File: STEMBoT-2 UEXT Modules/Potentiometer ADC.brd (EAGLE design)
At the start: 21.6 x 26.3 mm, 18 parts, among them IC1 74HC165PW,118, IC2 LMV324DR2G, IC3 LMV324DR2G, Q1 MMBT3904LP-7

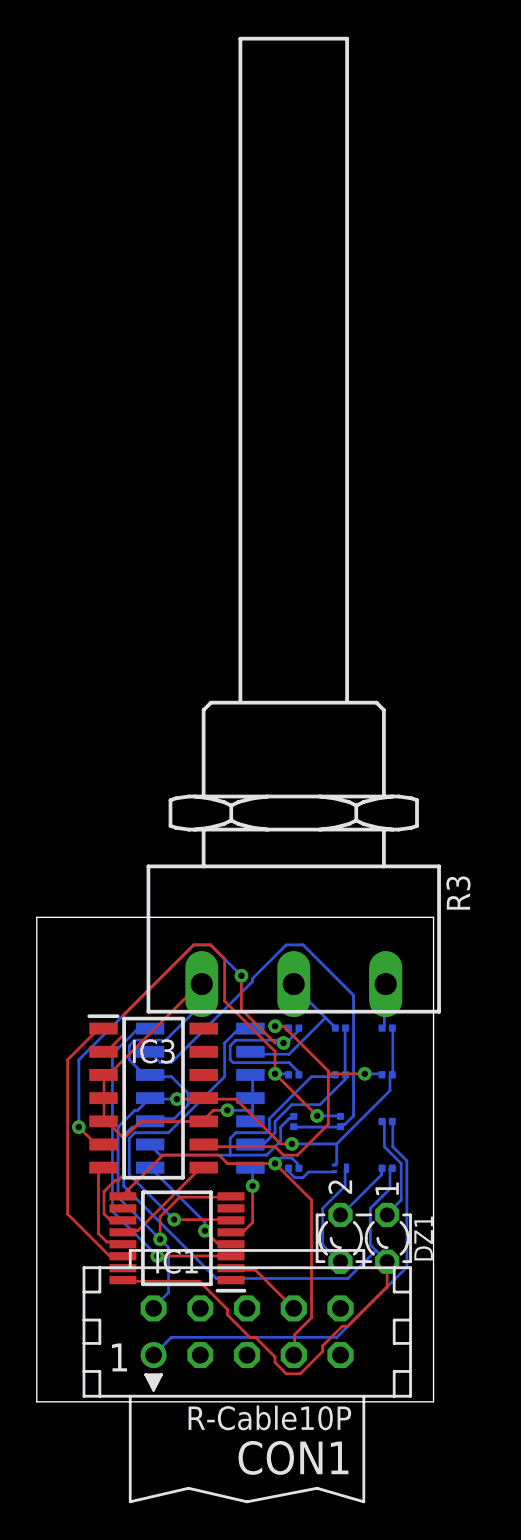
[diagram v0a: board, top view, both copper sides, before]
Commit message: Adjusted ADC modules for PCB order. Dan, these are auto-routed.
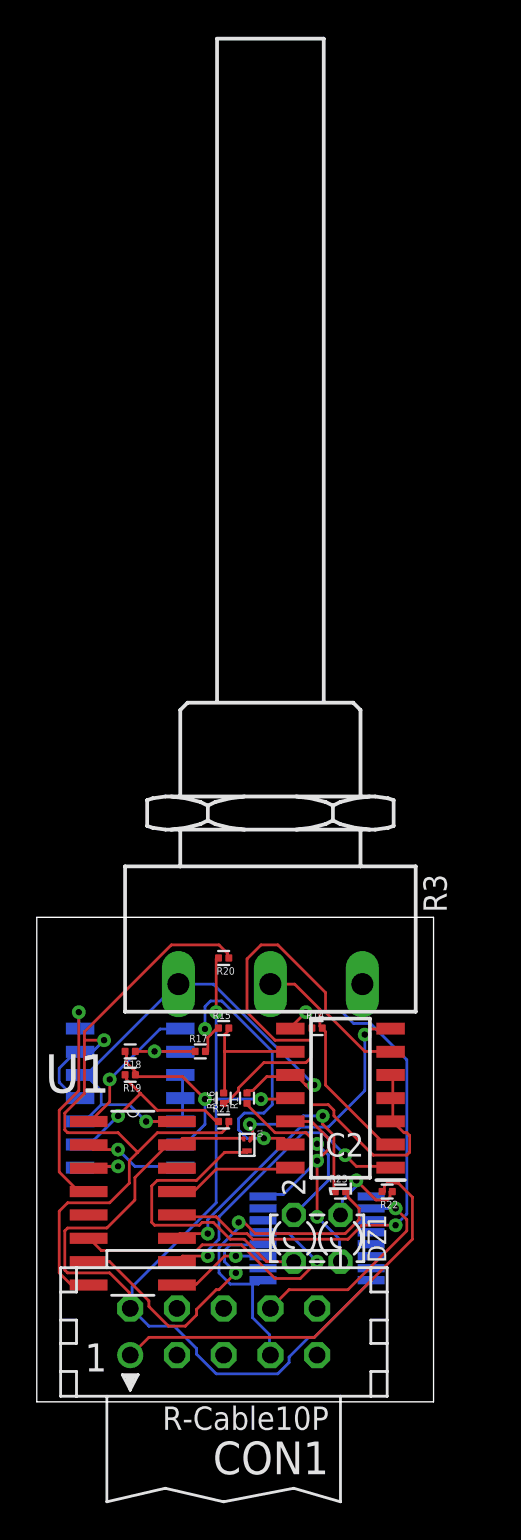
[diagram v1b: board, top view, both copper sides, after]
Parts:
- added U1: SN74HC148D, SN74HC148D:SOIC127P600X175-16N
- moved R20 9.67 mm to (10.2, 24.1), flipped to the top
- moved R19 9.25 mm to (5.08, 17.8), flipped to the top, turned to 180 degrees
- moved R21 9.25 mm to (10.2, 15.2), flipped to the top, turned to 0 degrees
- moved R18 8.98 mm to (5.08, 19.1), flipped to the top
- moved R17 8.52 mm to (8.89, 19.1), flipped to the top, turned to 0 degrees
- moved IC2 7.62 mm to (16.5, 16.5), flipped to the top, turned to 180 degrees
- moved IC1 7.62 mm to (15.2, 8.89), flipped to the bottom, turned to 0 degrees
- moved R16 6.48 mm to (10.2, 16.5), flipped to the top, turned to 90 degrees
- moved R15 6.35 mm to (10.2, 20.3), flipped to the top, turned to 0 degrees
- moved Q1 5.24 mm to (11.4, 14.0), flipped to the top, turned to 270 degrees
- moved R1 4.58 mm to (11.4, 16.5), flipped to the top, turned to 90 degrees
- moved R22 3.81 mm to (19.1, 11.4), flipped to the top
- moved R23 2.84 mm to (16.5, 11.4), flipped to the top
- moved DZ1 2.54 mm to (15.2, 8.89)
- moved R14 1.27 mm to (15.2, 20.3), flipped to the top
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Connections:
- removed net N$2 (its old number): CON1.2, IC1.8, IC2.11, IC3.11, Q1.2, R20.2, R21.2
- removed net N$27: CON1.7, IC1.9, R1.1
- removed net N$30: IC1.3, IC2.14
- new net N$12: CON1.2, IC1.8, IC2.11, Q1.2, R20.2, U1.15
- new net N$16: IC1.13, U1.6
- new net N$19: CON1.7, IC1.9, R23.2
- new net N$20: Q1.1, R23.1
- new net N$22: DZ1.A2, R1.1
- new net N$4: IC2.14, U1.13
- new net N$8: IC1.11, U1.9
- net N$1: now also IC3.11, IC3.13, R20.1, R21.2, U1.8; no longer Q1.1, R1.2
- net N$15: now also IC1.12, U1.7; no longer R20.1, R3.1A
- net N$23: now also U1.2; no longer IC1.13
- net N$26: now also U1.1; no longer IC1.14
- net N$31: now also U1.12; no longer IC1.4
- net N$32: now also U1.11; no longer IC1.5
- net N$33: now also U1.10; no longer IC1.6
- net N$5: now also IC3.12, R1.2, U1.16; no longer IC1.11, R23.1
- net N$6: now also U1.3; no longer IC1.12
- net N$7: now also IC3.14, U1.4; no longer DZ1.A2, R23.2
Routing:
- net N$12: track 0.00 -> 61.9 mm, vias 0 -> 2
- net N$1: track 3.08 -> 44.2 mm, vias 0 -> 1
- net N$2 (its old number): track 39.3 -> 0.00 mm, vias 3 -> 0
- net N$5: track 89.9 -> 62.0 mm, vias 1 -> 4
- net N$9: track 32.2 -> 9.28 mm, vias 3 -> 1
- net N$31: track 6.97 -> 29.8 mm, vias 1 -> 2
- net N$27: track 22.8 -> 0.00 mm, vias 1 -> 0
- net N$19: track 0.00 -> 19.8 mm, vias 0 -> 1
- net N$30: track 18.8 -> 0.00 mm, vias 1 -> 0
- net N$3: track 22.7 -> 4.66 mm, vias 2 -> 1
- net N$16: track 0.00 -> 17.6 mm, vias 0 -> 1
- net N$10: track 9.77 -> 25.7 mm
- net N$32: track 4.59 -> 18.6 mm, vias 1 -> 2
- net N$15: track 2.52 -> 14.7 mm, vias 0 -> 1
- net N$24: track 6.05 -> 16.7 mm
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
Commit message: Once again, updating ADC shematics and boards. Used autorouter.
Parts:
- removed IC2, IC3: LMV324DR2G, LMV324DR2G:SOP126P600X175-14N
- removed R20: ERJ-1RHD3601C, Resistor:RESC0603X26N
- added R2, R4: ERJ-1RHD3601C, Resistor:RESC0603X26N
- added U2, U3: MAX964ESET, MAX964ESET:SOIC127P600X175-16N
- moved R21 9.92 mm to (2.54, 21.6)
- moved R22 8.98 mm to (17.8, 2.54)
- moved R16 8.03 mm to (2.54, 19.1), turned to 180 degrees
- moved R18 5.68 mm to (10.2, 21.6)
- moved R23 5.39 mm to (20.3, 7.62), turned to 270 degrees
- moved R15 5.24 mm to (15.2, 21.6), turned to 180 degrees
- moved Q1 4.58 mm to (15.2, 11.4), turned to 180 degrees
- moved R17 4.58 mm to (5.08, 21.6)
- moved R14 3.81 mm to (15.2, 16.5), turned to 270 degrees
- moved R1 1.80 mm to (10.2, 15.2), turned to 180 degrees
- moved DZ1 1.27 mm to (15.2, 7.62)
- moved IC1 1.27 mm to (15.2, 10.2)
- moved R19 1.27 mm to (5.08, 19.1), turned to 0 degrees
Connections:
- removed net N$17: IC3.9, R19.2, R21.1
- removed net N$31: IC2.8, U1.12
- removed net N$32: IC2.7, U1.11
- removed net N$33: IC2.1, U1.10
- removed net N$5: DZ1.K1, IC1.16, IC2.10, IC2.12, IC2.3, IC2.4, IC2.5, IC3.10, IC3.12, IC3.3, IC3.4, IC3.5, R1.2, R3.1E, U1.16
- new net N$21: U1.2, U2.11
- new net N$27: U1.12, U3.14
- new net N$28: U1.11, U3.11
- new net N$29: U1.10, U3.10
- new net N$30: DZ1.K1, IC1.16, R1.2, R3.1E, R3.1S, R4.2, U1.16, U2.13, U2.2, U2.4, U2.6, U2.8, U3.13, U3.2, U3.4, U3.6, U3.8
- net N$1: now also R16.1, R2.2, U3.5; no longer IC3.11, IC3.13, R20.1, R21.2, U1.8
- net N$10: now also R16.2, R21.1, U3.3; no longer IC2.6, R14.1, R16.1
- net N$11: now also R19.1, R2.1, U3.7; no longer IC2.2, R14.2, R3.1S
- net N$12: now also R19.2, U1.8, U2.12, U3.12; no longer IC2.11, R20.2
- net N$13: now also U1.4, U2.15; no longer IC2.9, R15.2, R16.2
- net N$14: now also U1.3, U2.14; no longer IC2.13, R15.1, R17.2
- net N$23: now also U1.13, U2.10; no longer IC3.7, U1.2
- net N$26: now also U3.15; no longer IC3.1
- net N$3: now also R14.2, R4.1, U2.1; no longer IC3.2, R17.1, R18.1
- net N$4: now also R14.1, R15.1, U2.3; no longer IC2.14, U1.13
- net N$6: now also R15.2, R18.1, U2.5; no longer IC3.8, U1.3
- net N$7: now also R17.2, R18.2, U2.7; no longer IC3.14, U1.4
- net N$9: now also R17.1, R21.2, U3.1; no longer IC3.6, R18.2, R19.1
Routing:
- net N$30: track 0.00 -> 105.7 mm, vias 0 -> 1
- net N$5: track 62.0 -> 0.00 mm, vias 4 -> 0
- net N$3: track 4.66 -> 41.3 mm, vias 1 -> 3
- net N$1: track 44.2 -> 14.2 mm
- net N$31: track 29.8 -> 0.00 mm, vias 2 -> 0
- net N$32: track 18.6 -> 0.00 mm, vias 2 -> 0
- net N$33: track 16.2 -> 0.00 mm, vias 2 -> 0
- net N$29: track 0.00 -> 14.3 mm, vias 0 -> 1
- net N$10: track 25.7 -> 12.9 mm, vias 0 -> 1
- net N$6: track 3.74 -> 15.9 mm, vias 1 -> 0
- net N$28: track 0.00 -> 11.8 mm, vias 0 -> 1
- net N$21: track 0.00 -> 11.2 mm
- net N$24: track 16.7 -> 5.50 mm
- net N$17: track 10.7 -> 0.00 mm, vias 1 -> 0
- net N$2: track 22.6 -> 13.2 mm
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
